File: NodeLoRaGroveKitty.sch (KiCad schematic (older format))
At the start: 42 parts, among them IC1 CP2104, P1 PICKIT PROGRAMMER, P2 Battery, P3 USB_B, P4 A0, P5 D9, P6 I2C, Q1 MMBT2222A, Q2 MMBT2222A, SW1 SW_RESET, U1 AP2114, U2 MCP73831T-2ATI/OT, U3 ESP8266-12E

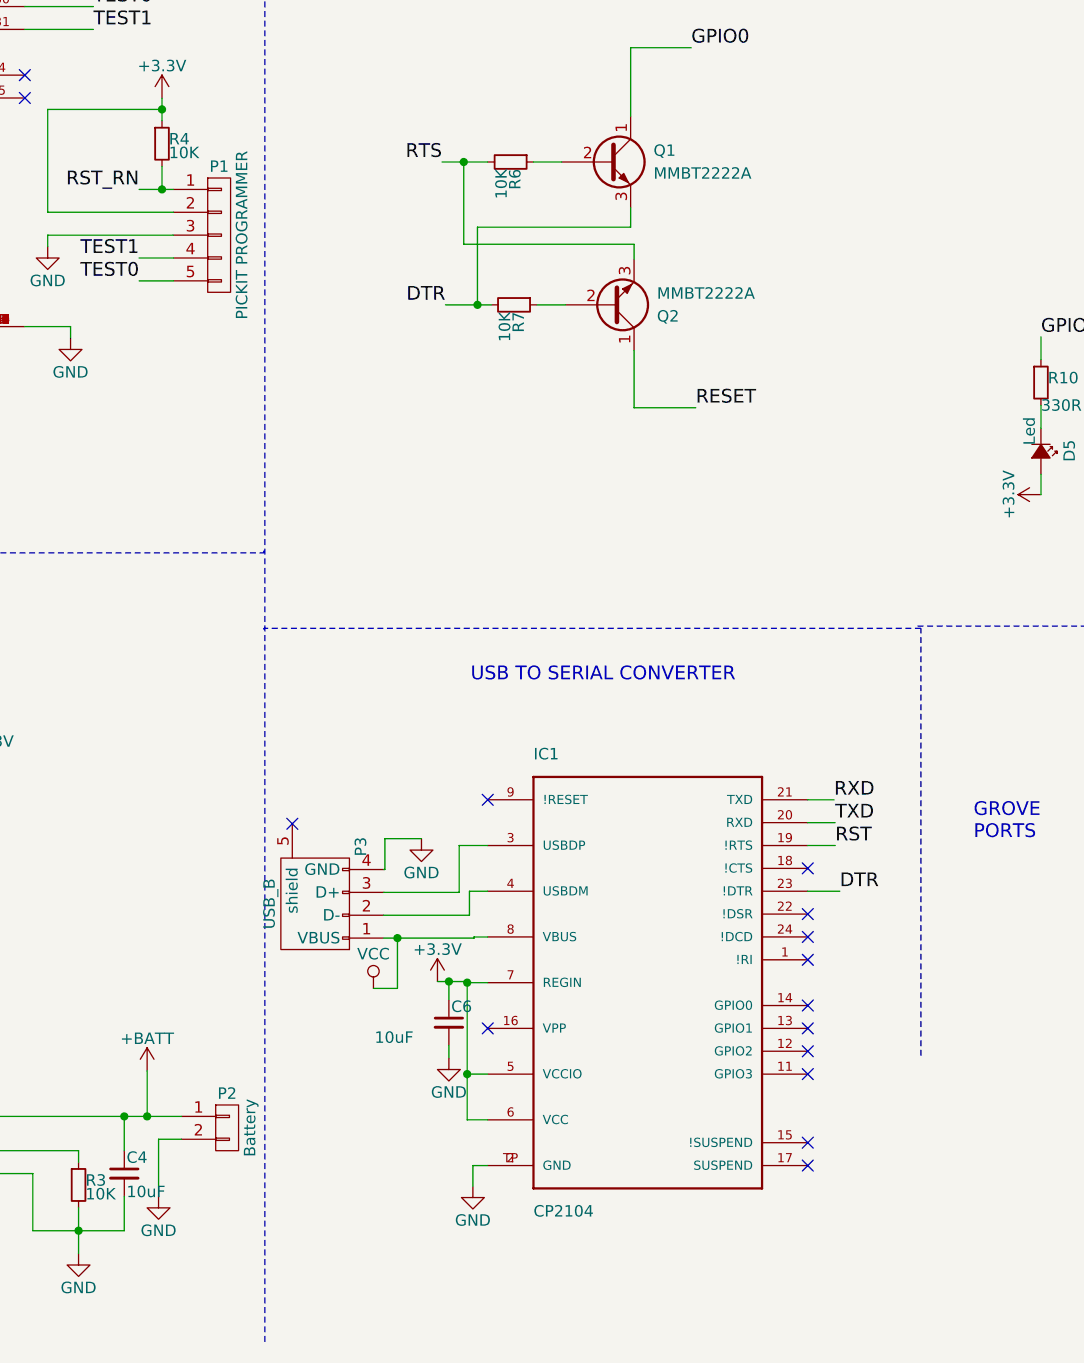
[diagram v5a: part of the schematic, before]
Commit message: Change USB with libraries
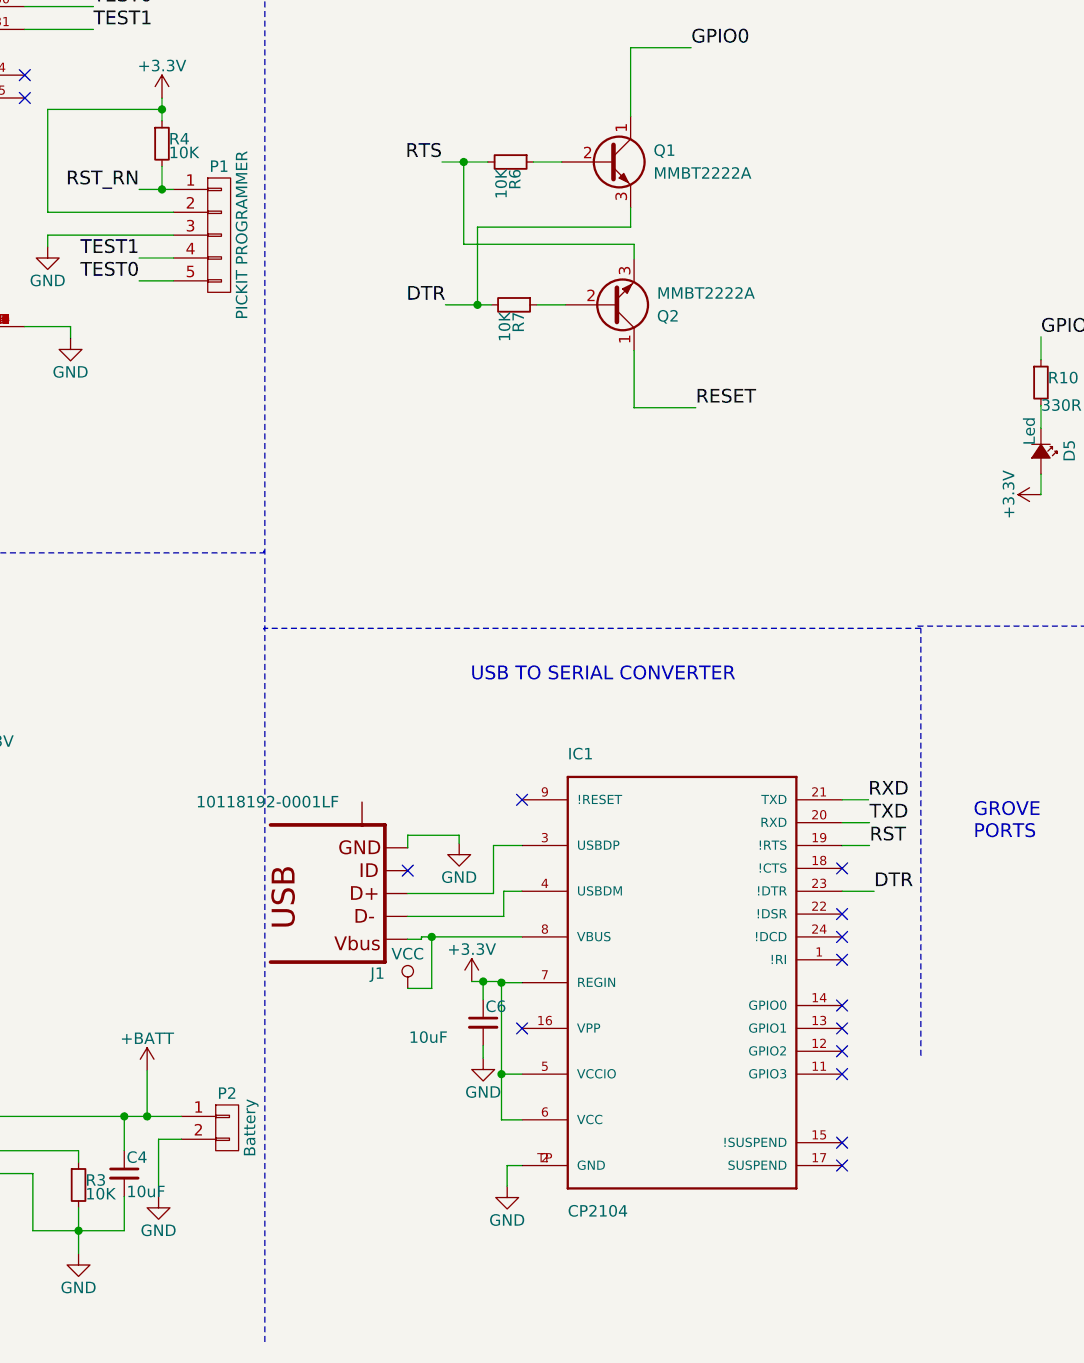
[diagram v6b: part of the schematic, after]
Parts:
- removed P3: USB_B, LoraCat:MOLEX_105017-0001, symbol USB_B
- added J1: 10118192-0001LF, 10118192-0001LF:10118192-0001LF, symbol 10118192-0001LF
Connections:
- net GND: now also J1.5 (GND)
- net VCC: now also J1.1 (VBUS)
- net at IC1.3 (USBDP): now also J1.3 (D+)
- net at IC1.4 (USBDM): now also J1.2 (D-)
- new net: J1.M1 (S), J1.M2 (S), J1.S1 (S), J1.S2 (S), J1.S3 (S), J1.S4 (S)
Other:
- moved on the sheet: C6, IC1
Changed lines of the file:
@@
 LIBS:contrib
 LIBS:valves
-LIBS:theinventorhouse
 LIBS:USB6B1
 LIBS:MCP73831T-2ATI_OT
-LIBS:antena_good
 LIBS:RN2903-I_RM095
-LIBS:ESP32-footprints-Shem-Lib
 LIBS:CP2104
 LIBS:NodeLoRaGroveKitty-cache
+LIBS:10118192-0001LF
 EELAYER 25 0
 EELAYER END
@@
 GPIO0
 $Comp
-L USB_B P3
-U 1 1 58A60EE9
-P 4320 5825
-F 0 "P3" H 4520 5625 50  0000 C CNN
-F 1 "USB_B" H 4270 6025 50  0000 C CNN
-F 2 "LoraCat:MOLEX_105017-0001" V 4270 5725 50  0001 C CNN
-F 3 "" V 4270 5725 50  0000 C CNN
-F 4 "105017-0001" H 4320 5825 60  0001 C CNN "manf#"
-	1    4320 5825
-	0    -1   -1   0
-$EndComp
-$Comp
 L CP2104 IC1
 U 1 1 58A6020A
-P 5775 6220
-F 0 "IC1" H 5275 7220 50  0000 L CNN
-F 1 "CP2104" H 5275 5220 50  0000 L CNN
-F 2 "Housings_DFN_QFN:QFN-24_4x4mm_Pitch0.5mm_NoMask" H 5775 6220 50  0001 L CNN
-F 3 "None" H 5775 6220 50  0001 L CNN
-F 4 "Silicon Labs" H 5775 6220 50  0001 L CNN "MF"
-F 5 "Unavailable" H 5775 6220 50  0001 L CNN "Availability"
-F 6 "CP2104" H 5775 6220 50  0001 L CNN "MP"
-F 7 "USB to UART Bridge" H 5775 6220 50  0001 L CNN "Description"
-F 8 "None" H 5775 6220 50  0001 L CNN "Package"
-F 9 "CP2104-F03-GM" H 5775 6220 60  0001 C CNN "manf#"
-	1    5775 6220
-	1    0    0    -1
-$EndComp
-NoConn ~ 5075 6420
+P 5925 6220
+F 0 "IC1" H 5425 7220 50  0000 L CNN
+F 1 "CP2104" H 5425 5220 50  0000 L CNN
+F 2 "Housings_DFN_QFN:QFN-24_4x4mm_Pitch0.5mm_NoMask" H 5925 6220 50  0001 L CNN
+F 3 "None" H 5925 6220 50  0001 L CNN
+F 4 "Silicon Labs" H 5925 6220 50  0001 L CNN "MF"
+F 5 "Unavailable" H 5925 6220 50  0001 L CNN "Availability"
+F 6 "CP2104" H 5925 6220 50  0001 L CNN "MP"
+F 7 "USB to UART Bridge" H 5925 6220 50  0001 L CNN "Description"
+F 8 "None" H 5925 6220 50  0001 L CNN "Package"
+F 9 "CP2104-F03-GM" H 5925 6220 60  0001 C CNN "manf#"
+	1    5925 6220
+	1    0    0    -1
+$EndComp
+NoConn ~ 5225 6420
 $Comp
 L +3.3V #PWR035
 U 1 1 58A65FBA
-P 4855 6215
-F 0 "#PWR035" H 4855 6065 50  0001 C CNN
-F 1 "+3.3V" H 4855 6355 50  0000 C CNN
-F 2 "" H 4855 6215 50  0000 C CNN
-F 3 "" H 4855 6215 50  0000 C CNN
-	1    4855 6215
+P 5005 6215
+F 0 "#PWR035" H 5005 6065 50  0001 C CNN
+F 1 "+3.3V" H 5005 6355 50  0000 C CNN
+F 2 "" H 5005 6215 50  0000 C CNN
+F 3 "" H 5005 6215 50  0000 C CNN
+	1    5005 6215
 	1    0    0    -1
 $EndComp
@@
 L C_Small C6
 U 1 1 58A664F1
-P 4905 6395
-F 0 "C6" H 4915 6465 50  0000 L CNN
-F 1 "10uF" H 4580 6330 50  0000 L CNN
-F 2 "Capacitors_SMD:C_0805_HandSoldering" H 4905 6395 50  0001 C CNN
-F 3 "" H 4905 6395 50  0000 C CNN
-F 4 "GRM21BR61A106KE19L" H 4905 6395 60  0001 C CNN "manf#"
-	1    4905 6395
+P 5055 6395
+F 0 "C6" H 5065 6465 50  0000 L CNN
+F 1 "10uF" H 4730 6330 50  0000 L CNN
+F 2 "Capacitors_SMD:C_0805_HandSoldering" H 5055 6395 50  0001 C CNN
+F 3 "" H 5055 6395 50  0000 C CNN
+F 4 "GRM21BR61A106KE19L" H 5055 6395 60  0001 C CNN "manf#"
+	1    5055 6395
 	1    0    0    -1
 $EndComp
@@
 L GND #PWR036
 U 1 1 58A66D85
-P 4905 6550
-F 0 "#PWR036" H 4905 6300 50  0001 C CNN
-F 1 "GND" H 4905 6400 50  0000 C CNN
-F 2 "" H 4905 6550 50  0000 C CNN
-F 3 "" H 4905 6550 50  0000 C CNN
-	1    4905 6550
-	1    0    0    -1
-$EndComp
-NoConn ~ 6475 5720
-NoConn ~ 6475 5920
-NoConn ~ 6475 6020
-NoConn ~ 6475 6120
-NoConn ~ 5075 5420
-NoConn ~ 6475 6920
-NoConn ~ 6475 7020
-NoConn ~ 6475 6620
-NoConn ~ 6475 6520
-NoConn ~ 6475 6420
-NoConn ~ 6475 6320
+P 5055 6550
+F 0 "#PWR036" H 5055 6300 50  0001 C CNN
+F 1 "GND" H 5055 6400 50  0000 C CNN
+F 2 "" H 5055 6550 50  0000 C CNN
+F 3 "" H 5055 6550 50  0000 C CNN
+	1    5055 6550
+	1    0    0    -1
+$EndComp
+NoConn ~ 6625 5720
+NoConn ~ 6625 5920
+NoConn ~ 6625 6020
+NoConn ~ 6625 6120
+NoConn ~ 5225 5420
+NoConn ~ 6625 6920
+NoConn ~ 6625 7020
+NoConn ~ 6625 6620
+NoConn ~ 6625 6520
+NoConn ~ 6625 6420
+NoConn ~ 6625 6320
 $Comp
 L GND #PWR037
 U 1 1 58A698FD
-P 5010 7110
-F 0 "#PWR037" H 5010 6860 50  0001 C CNN
-F 1 "GND" H 5010 6960 50  0000 C CNN
-F 2 "" H 5010 7110 50  0000 C CNN
-F 3 "" H 5010 7110 50  0000 C CNN
-	1    5010 7110
-	1    0    0    -1
-$EndComp
-Text Label 6615 5820 0    60   ~ 0
+P 5160 7110
+F 0 "#PWR037" H 5160 6860 50  0001 C CNN
+F 1 "GND" H 5160 6960 50  0000 C CNN
+F 2 "" H 5160 7110 50  0000 C CNN
+F 3 "" H 5160 7110 50  0000 C CNN
+	1    5160 7110
+	1    0    0    -1
+$EndComp
+Text Label 6765 5820 0    60   ~ 0
 DTR
-Text Label 6595 5520 0    60   ~ 0
+Text Label 6745 5520 0    60   ~ 0
 TXD
-Text Label 6590 5420 0    60   ~ 0
+Text Label 6740 5420 0    60   ~ 0
 RXD
-Text Label 6595 5620 0    60   ~ 0
+Text Label 6745 5620 0    60   ~ 0
 RST
 $Comp
 L VCC #PWR038
 U 1 1 58A6B1D3
-P 4575 6245
-F 0 "#PWR038" H 4575 6095 50  0001 C CNN
-F 1 "VCC" H 4575 6395 50  0000 C CNN
-F 2 "" H 4575 6245 50  0000 C CNN
-F 3 "" H 4575 6245 50  0000 C CNN
-	1    4575 6245
-	1    0    0    -1
-$EndComp
-$Comp
-L GND #PWR039
-U 1 1 58A6C294
-P 4785 5590
-F 0 "#PWR039" H 4785 5340 50  0001 C CNN
-F 1 "GND" H 4785 5440 50  0000 C CNN
-F 2 "" H 4785 5590 50  0000 C CNN
-F 3 "" H 4785 5590 50  0000 C CNN
-	1    4785 5590
+P 4725 6245
+F 0 "#PWR038" H 4725 6095 50  0001 C CNN
+F 1 "VCC" H 4725 6395 50  0000 C CNN
+F 2 "" H 4725 6245 50  0000 C CNN
+F 3 "" H 4725 6245 50  0000 C CNN
+	1    4725 6245
 	1    0    0    -1
 $EndComp
@@
 Text Label 4890 3255 2    60   ~ 0
 DTR
+Text Notes 5000 4910 0    60   ~ 0
+USB TO SERIAL CONVERTER
+NoConn ~ 4725 5730
+$Comp
+L 10118192-0001LF J1
+U 1 1 58ED66DB
+P 4425 5830
+F 0 "J1" H 4225 6180 50  0000 L CNN
+F 1 "10118192-0001LF" H 4425 5430 50  0000 L CNN
+F 2 "10118192-0001LF:10118192-0001LF" H 4425 5830 50  0001 L CNN
+F 3 "0.23 USD" H 4425 5830 50  0001 L CNN
+F 4 "FCI" H 4425 5830 50  0001 L CNN "MF"
+F 5 "Conn Micro USB Type B RCP 5 POS 0.65mm Solder RA SMD 5 Terminal 1 Port T/R" H 4425 5830 50  0001 L CNN "Description"
+F 6 "None" H 4425 5830 50  0001 L CNN "Package"
+F 7 "Good" H 4425 5830 50  0001 L CNN "Availability"
+F 8 "10118192-0001LF" H 4425 5830 50  0001 L CNN "MP"
+F 9 "10118192-0001LF" H 4425 5830 60  0001 C CNN "manf#"
+	1    4425 5830
+	-1   0    0    1
+$EndComp
+$Comp
+L GND #PWR039
+U 1 1 58EDBF39
+P 4950 5610
+F 0 "#PWR039" H 4950 5360 50  0001 C CNN
+F 1 "GND" H 4950 5460 50  0000 C CNN
+F 2 "" H 4950 5610 50  0000 C CNN
+F 3 "" H 4950 5610 50  0000 C CNN
+	1    4950 5610
+	1    0    0    -1
+$EndComp
 Wire Wire Line
 	7805 1485 7590 1485
@@
 	4095 4340 4095 4330
 Wire Wire Line
-	5075 5620 4950 5620
-Wire Wire Line
-	4950 5620 4950 5825
-Wire Wire Line
-	4950 5825 4620 5825
-Wire Wire Line
-	4995 5925 4995 5820
-Wire Wire Line
-	4620 5925 4995 5925
-Wire Wire Line
-	4995 5820 5075 5820
-Wire Wire Line
-	4620 6025 5015 6025
-Wire Wire Line
-	5015 6025 5015 6020
-Wire Wire Line
-	5015 6020 5075 6020
-Wire Wire Line
-	4985 6820 5075 6820
-Wire Wire Line
-	4985 6215 4985 6820
-Wire Wire Line
-	4985 6220 5075 6220
-Wire Wire Line
-	5075 6620 4985 6620
-Connection ~ 4985 6620
-Wire Wire Line
-	4855 6215 4985 6215
-Connection ~ 4985 6220
-Wire Wire Line
-	4905 6295 4905 6215
-Connection ~ 4905 6215
-Wire Wire Line
-	4905 6495 4905 6550
-Wire Wire Line
-	6475 5820 6615 5820
-Wire Wire Line
-	6475 5520 6595 5520
-Wire Wire Line
-	6475 5420 6590 5420
-Wire Wire Line
-	6475 5620 6595 5620
-Wire Wire Line
-	5075 7020 5010 7020
-Wire Wire Line
-	5010 7020 5010 7110
-Wire Wire Line
-	4575 6245 4680 6245
-Wire Wire Line
-	4680 6245 4680 6025
-Connection ~ 4680 6025
-Wire Wire Line
-	4785 5590 4625 5590
-Wire Wire Line
-	4625 5590 4625 5725
-Wire Wire Line
-	4625 5725 4620 5725
+	5100 5620 5100 5830
+Wire Wire Line
+	5145 5820 5145 5930
+Wire Wire Line
+	5145 5820 5225 5820
+Wire Wire Line
+	5135 6820 5225 6820
+Wire Wire Line
+	5135 6215 5135 6820
+Wire Wire Line
+	5135 6220 5225 6220
+Wire Wire Line
+	5225 6620 5135 6620
+Connection ~ 5135 6620
+Wire Wire Line
+	5005 6215 5135 6215
+Connection ~ 5135 6220
+Wire Wire Line
+	5055 6295 5055 6215
+Connection ~ 5055 6215
+Wire Wire Line
+	5055 6495 5055 6550
+Wire Wire Line
+	6625 5820 6765 5820
+Wire Wire Line
+	6625 5520 6745 5520
+Wire Wire Line
+	6625 5420 6740 5420
+Wire Wire Line
+	6625 5620 6745 5620
+Wire Wire Line
+	5225 7020 5160 7020
+Wire Wire Line
+	5160 7020 5160 7110
+Wire Wire Line
+	4830 6245 4725 6245
+Wire Wire Line
+	4830 6020 4830 6245
 Wire Wire Line
 	5415 3255 5290 3255
 Wire Wire Line
-	5090 3255 4890 3255
+	4890 3255 5090 3255
 Wire Wire Line
 	5400 2630 5275 2630
 Wire Wire Line
-	5075 2630 4875 2630
+	4875 2630 5075 2630
 Wire Wire Line
 	5700 2830 5700 2915
@@
 Wire Notes Line
 	4095 4670 4095 4675
-Text Notes 5000 4910 0    60   ~ 0
-USB TO SERIAL CONVERTER
-NoConn ~ 4220 5525
+Wire Wire Line
+	4950 5575 4950 5610
+Wire Wire Line
+	5225 5620 5100 5620
+Wire Wire Line
+	5100 5830 4725 5830
+Wire Wire Line
+	5145 5930 4725 5930
+Wire Wire Line
+	4785 6020 5225 6020
+Wire Wire Line
+	4725 6030 4785 6030
+Wire Wire Line
+	4785 6030 4785 6020
+Connection ~ 4830 6020
+Wire Wire Line
+	4725 5575 4725 5630
+Wire Wire Line
+	4950 5575 4725 5575
 $EndSCHEMATC

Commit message: Add #maf to battery conector
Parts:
- P2: #manf (none) -> S2B-PH-SM4-TB(LF)(SN)
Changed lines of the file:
@@
 F 2 "modules:panelmate_smd_2" H 3935 6855 50  0001 C CNN
 F 3 "" H 3935 6855 50  0000 C CNN
+F 4 "S2B-PH-SM4-TB(LF)(SN)" H 3935 6855 60  0001 C CNN "#manf"
 	1    3935 6855
 	1    0    0    -1

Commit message: Add new RN and fix ways
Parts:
- MODULE1: manf# RN2903-I/RM095 -> RN2903A-I/RM098
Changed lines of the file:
@@
 F 7 "RN2483-I/RM095" H 2250 2150 50  0001 L CNN "MP"
 F 8 "Bad" H 2250 2150 50  0001 L CNN "Availability"
-F 9 "RN2903-I/RM095" H 2250 2150 60  0001 C CNN "manf#"
+F 9 "RN2903A-I/RM098" H 2250 2150 60  0001 C CNN "manf#"
 	1    2250 2150
 	1    0    0    -1
